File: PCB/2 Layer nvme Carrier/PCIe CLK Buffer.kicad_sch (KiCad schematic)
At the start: 19 parts

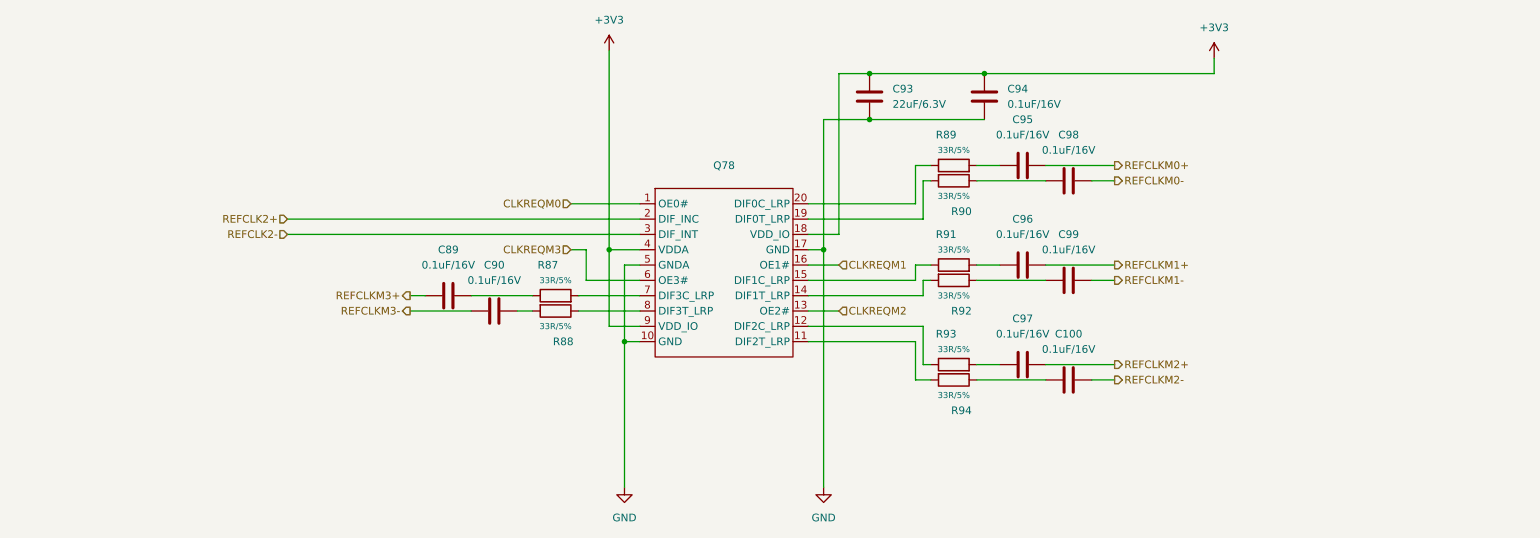
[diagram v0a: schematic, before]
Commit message: PCIe and CLK Buffenr Lines
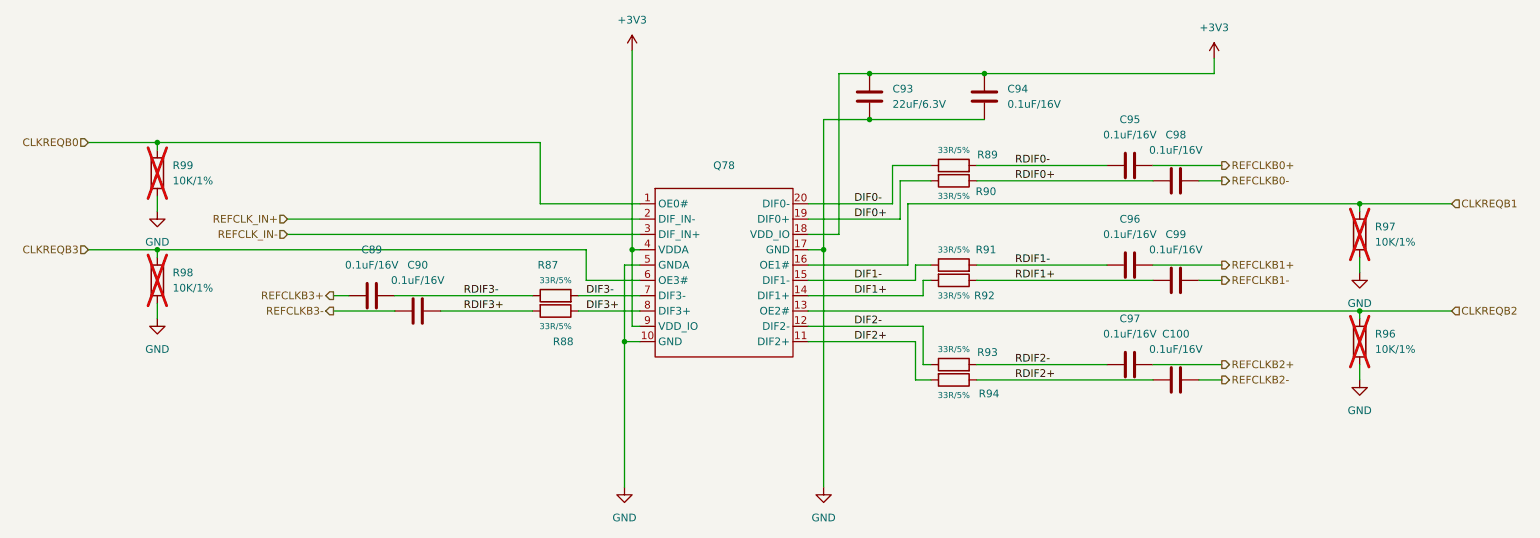
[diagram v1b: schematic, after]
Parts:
- added R96, R97, R98, R99: 10K/1%, Resistor_SMD:R_0402_1005Metric, symbol Device:R
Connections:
- net GND: now also R96.2, R97.2, R98.2, R99.2
- net RDIF2+: now reaches C100.1, R94.1
- net DIF2+: now reaches Q78.11 (DIF2+), R94.2
- net DIF1-: now reaches Q78.15 (DIF1-), R91.1
- net RDIF1-: now reaches C96.1, R91.2
- net DIF2-: now reaches Q78.12 (DIF2-), R93.1
- net RDIF2-: now reaches C97.1, R93.2
- net RDIF1+: now reaches C99.1, R92.1
- net DIF1+: now reaches Q78.14 (DIF1+), R92.2
- net DIF3+: now reaches Q78.8 (DIF3+), R88.1
- net RDIF3+: now reaches C90.2, R88.2
- net RDIF3-: now reaches C89.2, R87.1
- net RDIF0+: now reaches C98.1, R90.1
- net DIF0+: now reaches Q78.19 (DIF0+), R90.2
- net RDIF0-: now reaches C95.1, R89.2
- net DIF0-: now reaches Q78.20 (DIF0-), R89.1
- net DIF3-: now reaches Q78.7 (DIF3-), R87.2
- net CLKREQM0 renamed CLKREQB0
- net CLKREQB0: now also R99.1
- net CLKREQM1 renamed CLKREQB1
- net CLKREQB1: now also R97.1
- net CLKREQM2 renamed CLKREQB2
- net CLKREQB2: now also R96.1
- net CLKREQM3 renamed CLKREQB3
- net CLKREQB3: now also R98.1
- net REFCLK2+ renamed REFCLK_IN+
- net REFCLK2- renamed REFCLK_IN-
- net REFCLKM0+ renamed REFCLKB0+
- net REFCLKM0- renamed REFCLKB0-
- net REFCLKM1+ renamed REFCLKB1+
- net REFCLKM1- renamed REFCLKB1-
- net REFCLKM2+ renamed REFCLKB2+
- net REFCLKM2- renamed REFCLKB2-
- net REFCLKM3+ renamed REFCLKB3+
- net REFCLKM3- renamed REFCLKB3-
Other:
- moved on the sheet: C100, C89, C90, C95, C96, C97, C98, C99

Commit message: Work
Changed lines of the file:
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@@
 		(on_board yes)
 		(dnp no)
-		(fields_autoplaced yes)
 		(property "Reference" "C100"
-			(at 219.71 102.87 90)
+			(at 222.504 103.378 90)
 			(effects
 				(font
@@
 		(on_board yes)
 		(dnp no)
-		(fields_autoplaced yes)
 		(property "Reference" "C99"
-			(at 219.71 86.36 90)
+			(at 222.25 86.36 90)
 			(effects
 				(font
@@
 		(on_board yes)
 		(dnp no)
-		(fields_autoplaced yes)
 		(property "Reference" "C89"
-			(at 86.36 88.9 90)
+			(at 82.804 94.488 90)
 			(effects
 				(font
@@
 		(on_board yes)
 		(dnp no)
-		(fields_autoplaced yes)
 		(property "Reference" "C98"
-			(at 219.71 69.85 90)
+			(at 222.25 69.85 90)
 			(effects
 				(font
@@
 		(on_board yes)
 		(dnp no)
-		(fields_autoplaced yes)
 		(property "Reference" "C90"
-			(at 93.98 91.44 90)
-			(effects
-				(font
+			(at 98.044 101.6 90)
+			(effects
+				(font
